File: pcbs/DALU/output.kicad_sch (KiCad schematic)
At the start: 31 parts, among them U801 74HC74, U802 74HC32, U803 74HCT574

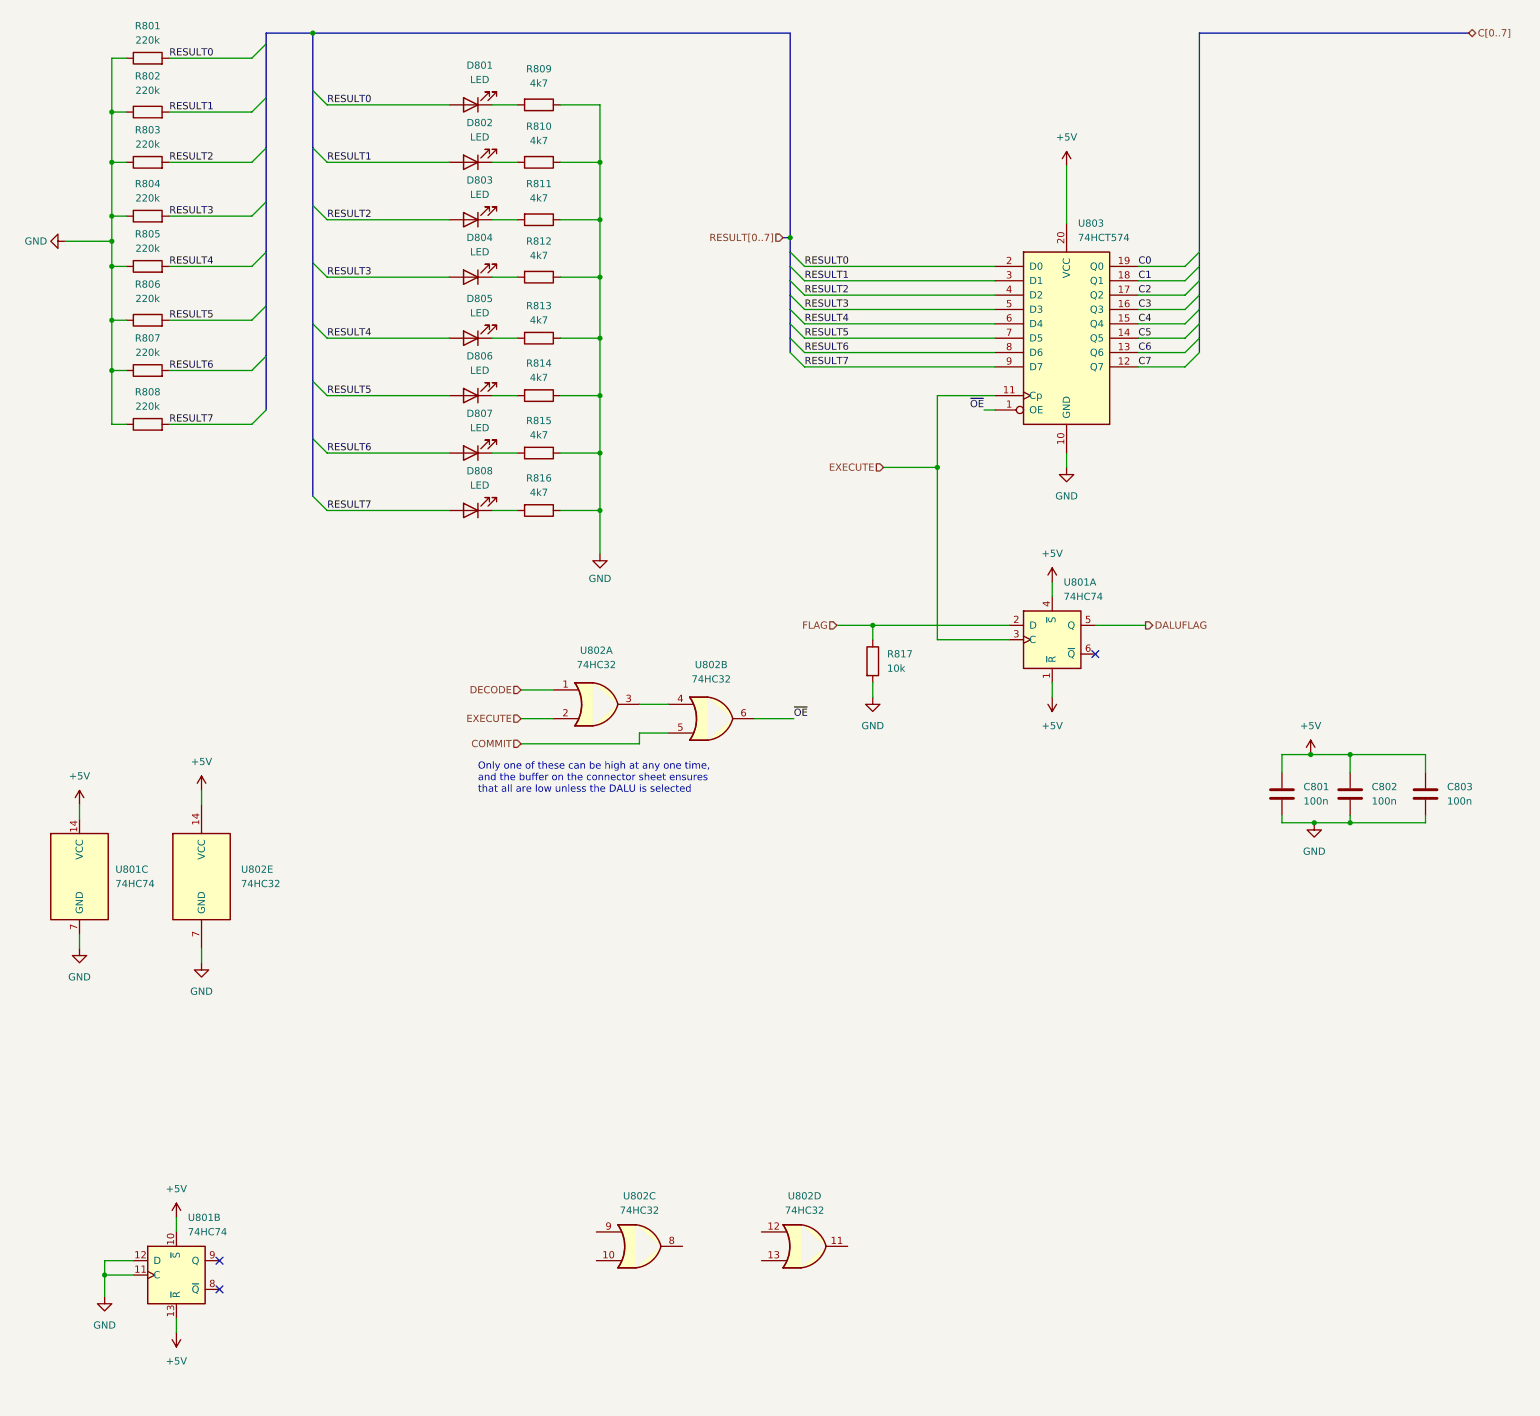
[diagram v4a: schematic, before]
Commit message: Forgot to invert the ORs in the output stage....
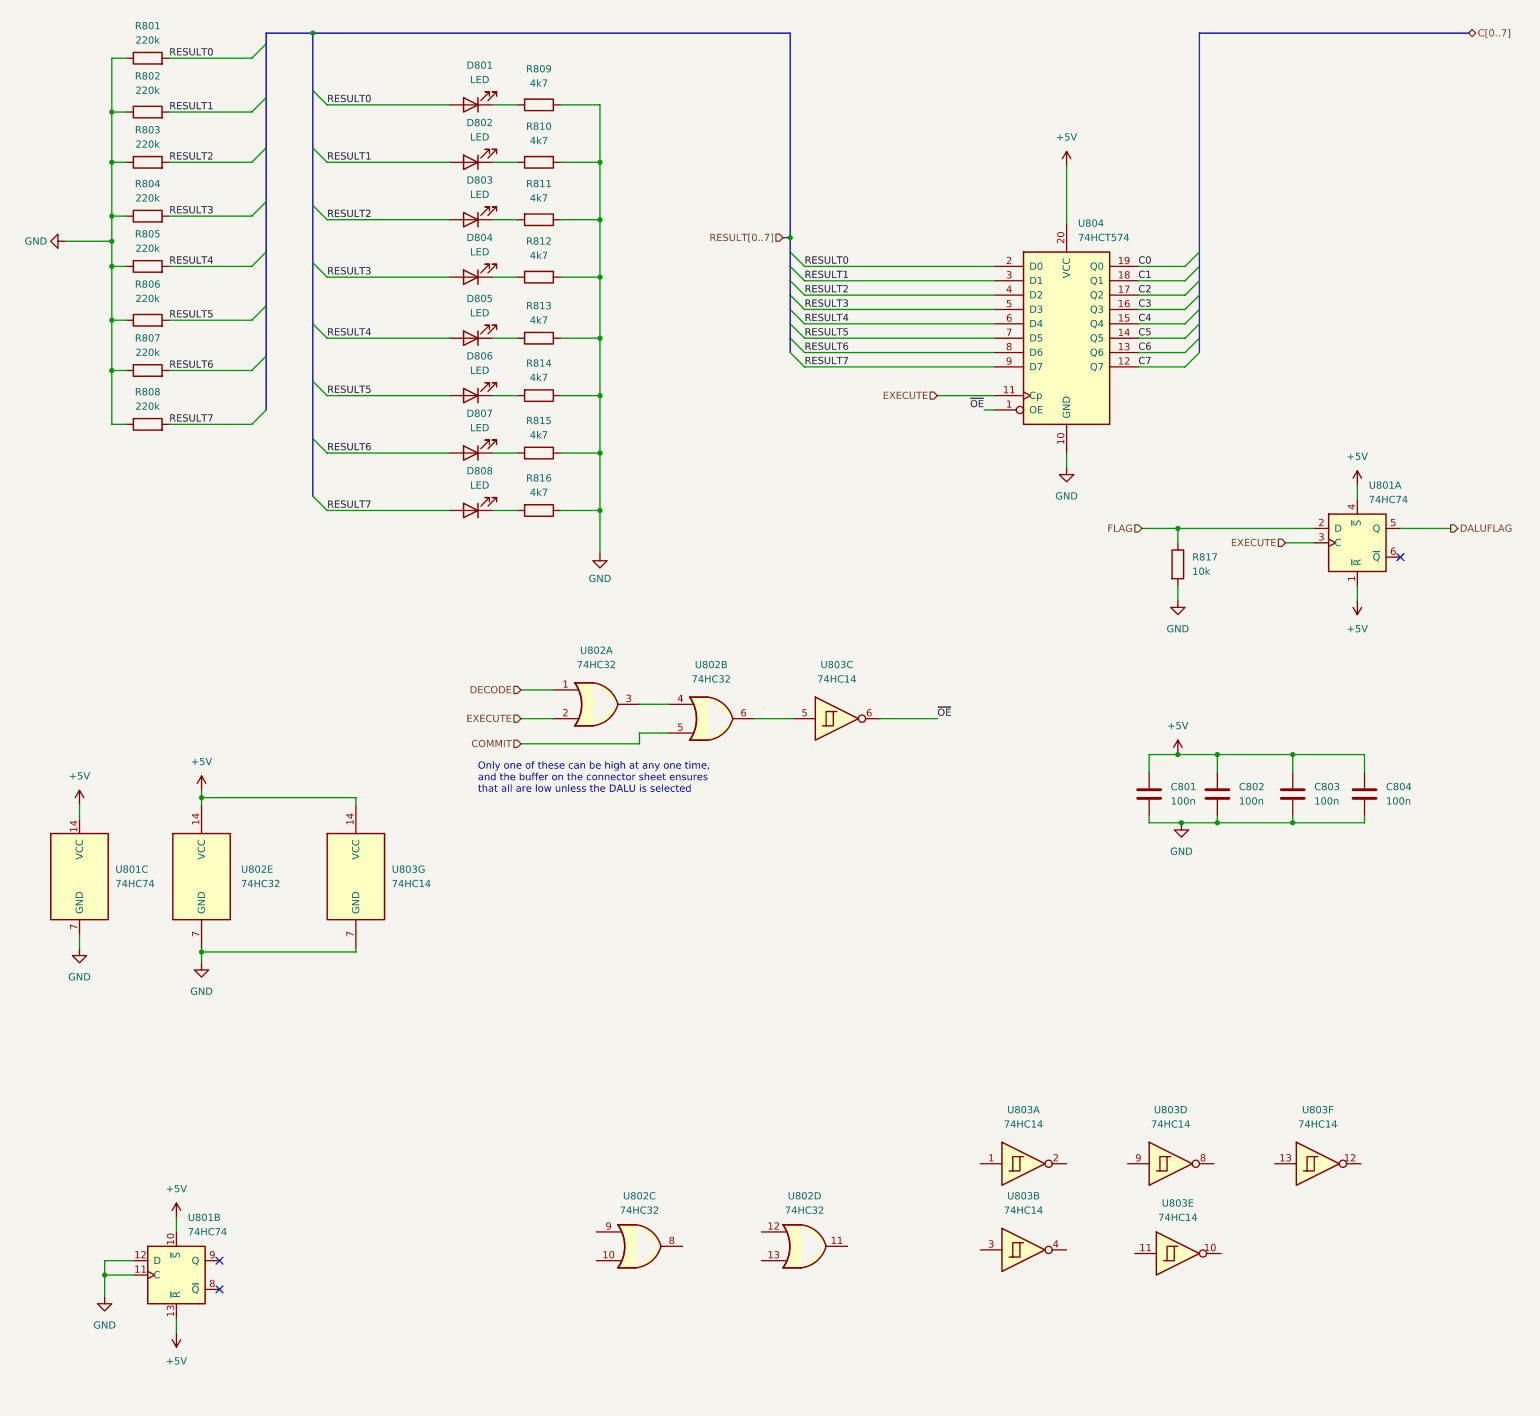
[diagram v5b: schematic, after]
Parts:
- added C804: 100n, Capacitor_SMD:C_0603_1608Metric, symbol Device:C
- added U803: 74HC14, symbol 74xx:74HC14
- renumbered U803 to U804
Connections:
- net +5V: now also C804.1, U803.14 (VCC)
- net GND: now also C804.2, U803.7 (GND)
- net ~{OE}: now also U803.6; no longer U802.6
- new net: U802.6, U803.5
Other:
- moved on the sheet: C801, C802, C803, R817, U801A

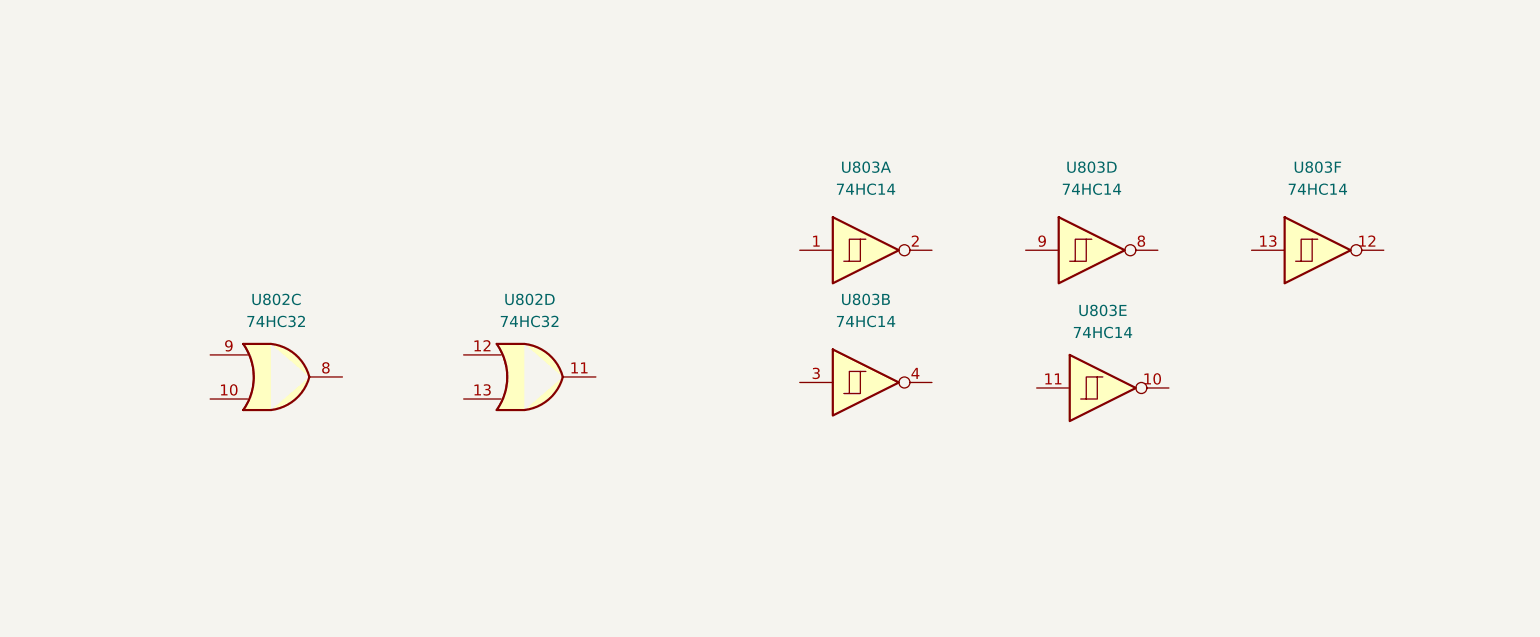
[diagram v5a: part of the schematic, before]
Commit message: Filling out connections
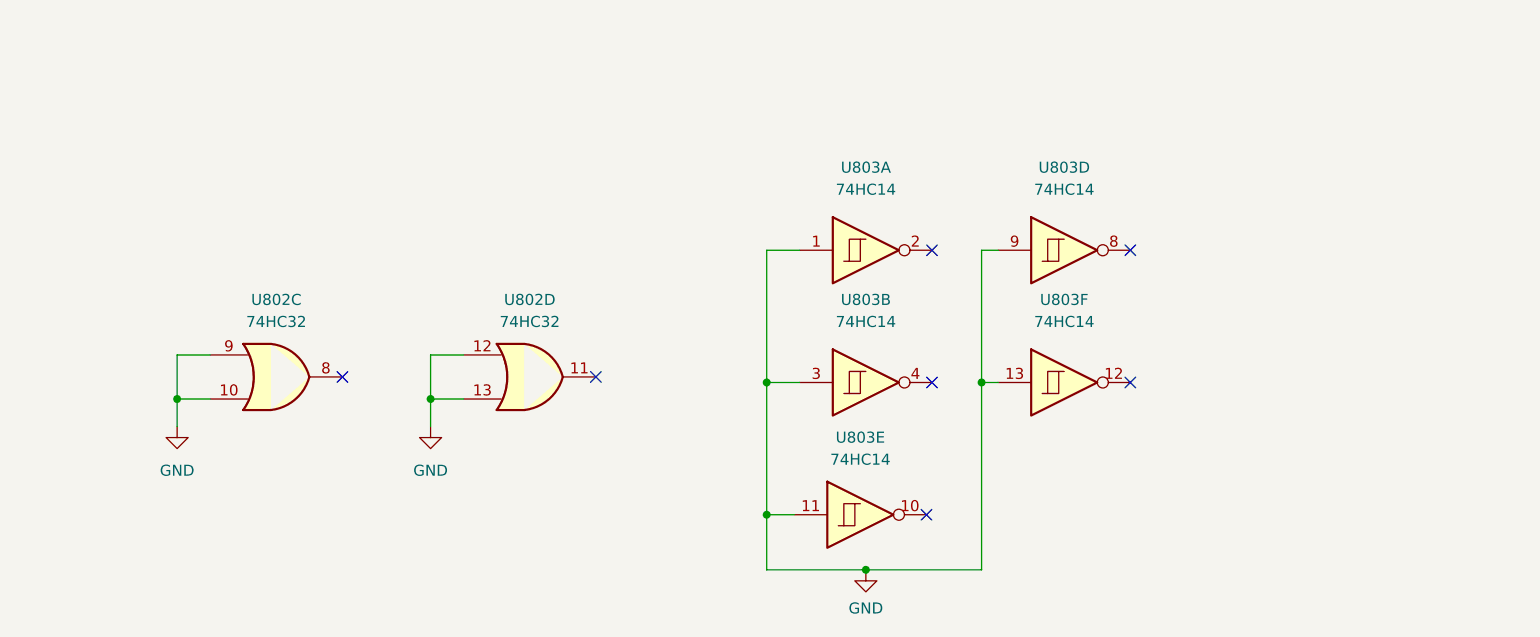
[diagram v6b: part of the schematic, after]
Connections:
- net GND: now also U802.10, U802.12, U802.13, U802.9, U803.1, U803.11, U803.13, U803.3, U803.9
- no-connect marks 3 -> 10
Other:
- moved on the sheet: U803D, U803E, U803F

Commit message: Sending for production
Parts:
- D801, D802, D803, D804, D805, D806, D807, D808: value LED -> GREEN
- U801, U802, U804: now left out of the parts list
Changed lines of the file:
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@@
     (in_bom yes) (on_board yes) (fields_autoplaced)
     (property "Reference" "D801" (id 0) (at 99.3775 22.225 0))
-    (property "Value" "LED" (id 1) (at 99.3775 24.765 0))
+    (property "Value" "GREEN" (id 1) (at 99.3775 24.765 0))
     (property "Footprint" "LED_SMD:LED_0603_1608Metric" (id 2) (at 97.79 29.21 0)
       (effects (font (size 1.27 1.27)) hide)
@@
   )
   (symbol (lib_id "74xx:74LS32") (at 140.335 137.795 0) (unit 2)
-    (in_bom yes) (on_board yes) (fields_autoplaced)
+    (in_bom no) (on_board yes) (fields_autoplaced)
     (property "Reference" "U802" (id 0) (at 140.335 128.27 0))
     (property "Value" "74HC32" (id 1) (at 140.335 130.81 0))
@@
   )
   (symbol (lib_id "74xx:74HC74") (at 254.635 106.68 0) (unit 1)
-    (in_bom yes) (on_board yes) (fields_autoplaced)
+    (in_bom no) (on_board yes) (fields_autoplaced)
     (property "Reference" "U801" (id 0) (at 256.6544 96.52 0)
       (effects (font (size 1.27 1.27)) (justify left))
@@
     (in_bom yes) (on_board yes) (fields_autoplaced)
     (property "Reference" "D805" (id 0) (at 99.3775 63.5 0))
-    (property "Value" "LED" (id 1) (at 99.3775 66.04 0))
+    (property "Value" "GREEN" (id 1) (at 99.3775 66.04 0))
     (property "Footprint" "LED_SMD:LED_0603_1608Metric" (id 2) (at 97.79 70.485 0)
       (effects (font (size 1.27 1.27)) hide)
@@
   )
   (symbol (lib_id "74xx:74HC74") (at 28.575 165.735 0) (unit 3)
-    (in_bom yes) (on_board yes) (fields_autoplaced)
+    (in_bom no) (on_board yes) (fields_autoplaced)
     (property "Reference" "U801" (id 0) (at 34.925 164.4649 0)
       (effects (font (size 1.27 1.27)) (justify left))
@@
   )
   (symbol (lib_id "74xx:74LS32") (at 120.015 135.255 0) (unit 1)
-    (in_bom yes) (on_board yes) (fields_autoplaced)
+    (in_bom no) (on_board yes) (fields_autoplaced)
     (property "Reference" "U802" (id 0) (at 120.015 125.73 0))
     (property "Value" "74HC32" (id 1) (at 120.015 128.27 0))
@@
     (in_bom yes) (on_board yes) (fields_autoplaced)
     (property "Reference" "D802" (id 0) (at 99.3775 32.385 0))
-    (property "Value" "LED" (id 1) (at 99.3775 34.925 0))
+    (property "Value" "GREEN" (id 1) (at 99.3775 34.925 0))
     (property "Footprint" "LED_SMD:LED_0603_1608Metric" (id 2) (at 97.79 39.37 0)
       (effects (font (size 1.27 1.27)) hide)
@@
     (in_bom yes) (on_board yes) (fields_autoplaced)
     (property "Reference" "D808" (id 0) (at 99.3775 93.98 0))
-    (property "Value" "LED" (id 1) (at 99.3775 96.52 0))
+    (property "Value" "GREEN" (id 1) (at 99.3775 96.52 0))
     (property "Footprint" "LED_SMD:LED_0603_1608Metric" (id 2) (at 97.79 100.965 0)
       (effects (font (size 1.27 1.27)) hide)
@@
     (in_bom yes) (on_board yes) (fields_autoplaced)
     (property "Reference" "D807" (id 0) (at 99.3775 83.82 0))
-    (property "Value" "LED" (id 1) (at 99.3775 86.36 0))
+    (property "Value" "GREEN" (id 1) (at 99.3775 86.36 0))
     (property "Footprint" "LED_SMD:LED_0603_1608Metric" (id 2) (at 97.79 90.805 0)
       (effects (font (size 1.27 1.27)) hide)
@@
     (in_bom yes) (on_board yes) (fields_autoplaced)
     (property "Reference" "D806" (id 0) (at 99.3775 73.66 0))
-    (property "Value" "LED" (id 1) (at 99.3775 76.2 0))
+    (property "Value" "GREEN" (id 1) (at 99.3775 76.2 0))
     (property "Footprint" "LED_SMD:LED_0603_1608Metric" (id 2) (at 97.79 80.645 0)
       (effects (font (size 1.27 1.27)) hide)
@@
     (in_bom yes) (on_board yes) (fields_autoplaced)
     (property "Reference" "D803" (id 0) (at 99.3775 42.545 0))
-    (property "Value" "LED" (id 1) (at 99.3775 45.085 0))
+    (property "Value" "GREEN" (id 1) (at 99.3775 45.085 0))
     (property "Footprint" "LED_SMD:LED_0603_1608Metric" (id 2) (at 97.79 49.53 0)
       (effects (font (size 1.27 1.27)) hide)
@@
   )
   (symbol (lib_id "74xx:74HC74") (at 45.72 236.22 0) (unit 2)
-    (in_bom yes) (on_board yes) (fields_autoplaced)
+    (in_bom no) (on_board yes) (fields_autoplaced)
     (property "Reference" "U801" (id 0) (at 47.7394 226.06 0)
       (effects (font (size 1.27 1.27)) (justify left))
@@
   )
   (symbol (lib_id "74xx:74LS32") (at 156.845 231.14 0) (unit 4)
-    (in_bom yes) (on_board yes) (fields_autoplaced)
+    (in_bom no) (on_board yes) (fields_autoplaced)
     (property "Reference" "U802" (id 0) (at 156.845 222.25 0))
     (property "Value" "74HC32" (id 1) (at 156.845 224.79 0))
@@
   )
   (symbol (lib_id "74xx:74LS32") (at 50.165 165.735 0) (unit 5)
-    (in_bom yes) (on_board yes) (fields_autoplaced)
+    (in_bom no) (on_board yes) (fields_autoplaced)
     (property "Reference" "U802" (id 0) (at 57.15 164.4649 0)
       (effects (font (size 1.27 1.27)) (justify left))
@@
   )
   (symbol (lib_id "74xx:74HCT574") (at 203.2 70.485 0) (unit 1)
-    (in_bom yes) (on_board yes) (fields_autoplaced)
+    (in_bom no) (on_board yes) (fields_autoplaced)
     (property "Reference" "U804" (id 0) (at 205.2194 50.165 0)
       (effects (font (size 1.27 1.27)) (justify left))
@@
     (in_bom yes) (on_board yes) (fields_autoplaced)
     (property "Reference" "D804" (id 0) (at 99.3775 52.705 0))
-    (property "Value" "LED" (id 1) (at 99.3775 55.245 0))
+    (property "Value" "GREEN" (id 1) (at 99.3775 55.245 0))
     (property "Footprint" "LED_SMD:LED_0603_1608Metric" (id 2) (at 97.79 59.69 0)
       (effects (font (size 1.27 1.27)) hide)
@@
   )
   (symbol (lib_id "74xx:74LS32") (at 127.635 231.14 0) (unit 3)
-    (in_bom yes) (on_board yes) (fields_autoplaced)
+    (in_bom no) (on_board yes) (fields_autoplaced)
     (property "Reference" "U802" (id 0) (at 127.635 222.25 0))
     (property "Value" "74HC32" (id 1) (at 127.635 224.79 0))
